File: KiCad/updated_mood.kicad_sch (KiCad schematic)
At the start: 11 parts, among them J3 Conn_01x02, J5 Conn_01x03, J6 Conn_01x02, U1 L293

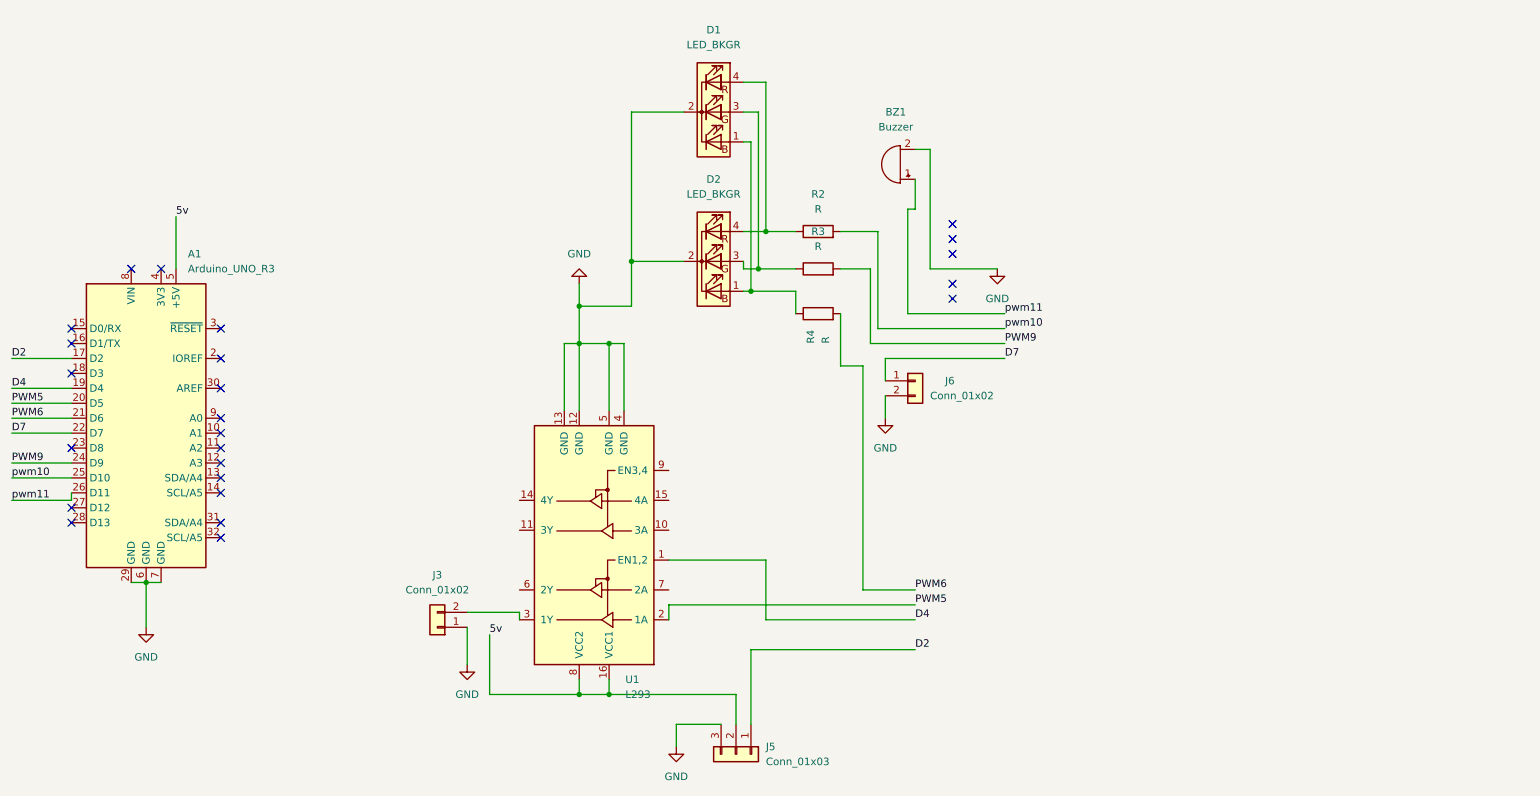
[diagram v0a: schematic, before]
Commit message: cleaning up
* removed second RGB led
* cleaned up circuit diagram
* added notes to KiCAD README
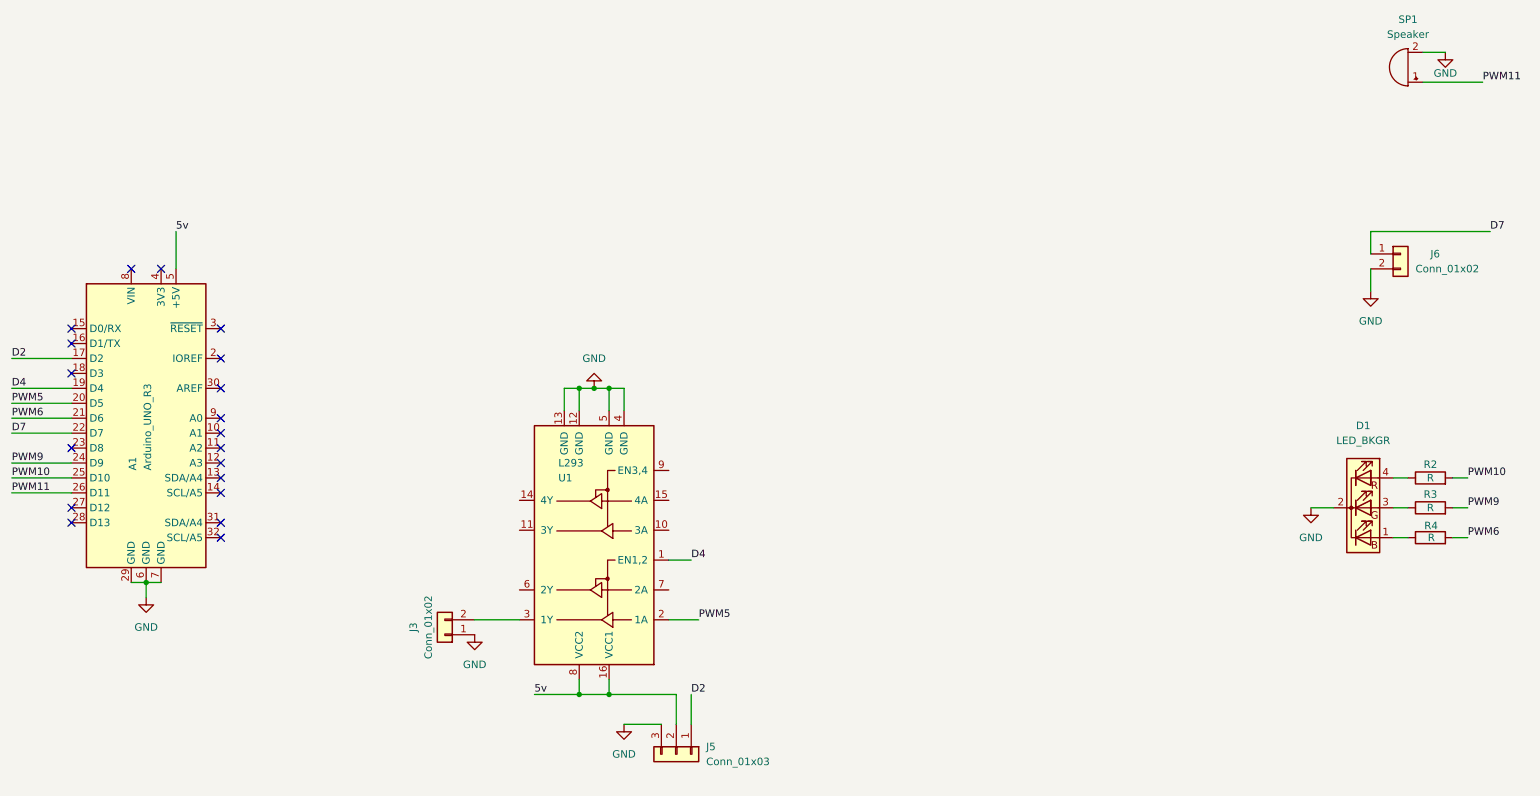
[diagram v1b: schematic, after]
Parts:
- removed D1: LED_BKGR, LED_THT:LED_D5.0mm-4_RGB_Wide_Pins, symbol Device:LED_BKGR
- SP1: renamed from BZ1; value Buzzer -> Speaker
- renumbered D2 to D1
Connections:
- net pwm10 renamed PWM10
- net pwm11 renamed PWM11
- no-connect marks 24 -> 19
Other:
- moved on the sheet: D1, J3, J5, J6, R2, R3, R4, SP1
